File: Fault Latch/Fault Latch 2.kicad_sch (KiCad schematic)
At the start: 113 parts, among them J1 1053141312, J3 1053131202, J4 1053131202, J5 1053131202, K3 Fujitsu_FTR-LYCA005x, K5 Fujitsu_FTR-LYCA005x, K6 Fujitsu_FTR-LYCA005x, Q101 Q_NPN_BEC, Q102 Q_NPN_BEC, Q103 Q_NPN_BEC, Q104 Q_NPN_BEC, Q105 Q_NMOS_GSD, Q106 Q_NMOS_GSD, Q110 Q_NPN_BEC, Q111 Q_NPN_BEC, Q112 Q_NMOS_GSD, Q113 Q_NMOS_GSD, Q114 Q_NMOS_GSD, Q115 Q_NMOS_GSD, Q117 Q_NMOS_GSD, Q118 Q_NMOS_GSD, Q119 Q_NMOS_GSD, Q120 Q_NMOS_GSD, Q121 Q_NMOS_GSD, Q122 Q_NMOS_GSD, Q123 Q_NMOS_GSD, Q124 Q_NMOS_GSD, Q125 Q_NMOS_GSD, SW101 SW_Omron_B3FS, SW102 SW_Omron_B3FS, SW103 SW_Omron_B3FS, U1 74LS279, U104 74AHC1G00, U109 74AHC1G00, U112 74AHC1G00, U117 74AHC1G00, U118 LM555xM, U2 LM1117DT-5.0, U7 SN74AHC1G08DBVR, U8 SN74AHC1G08DBVR

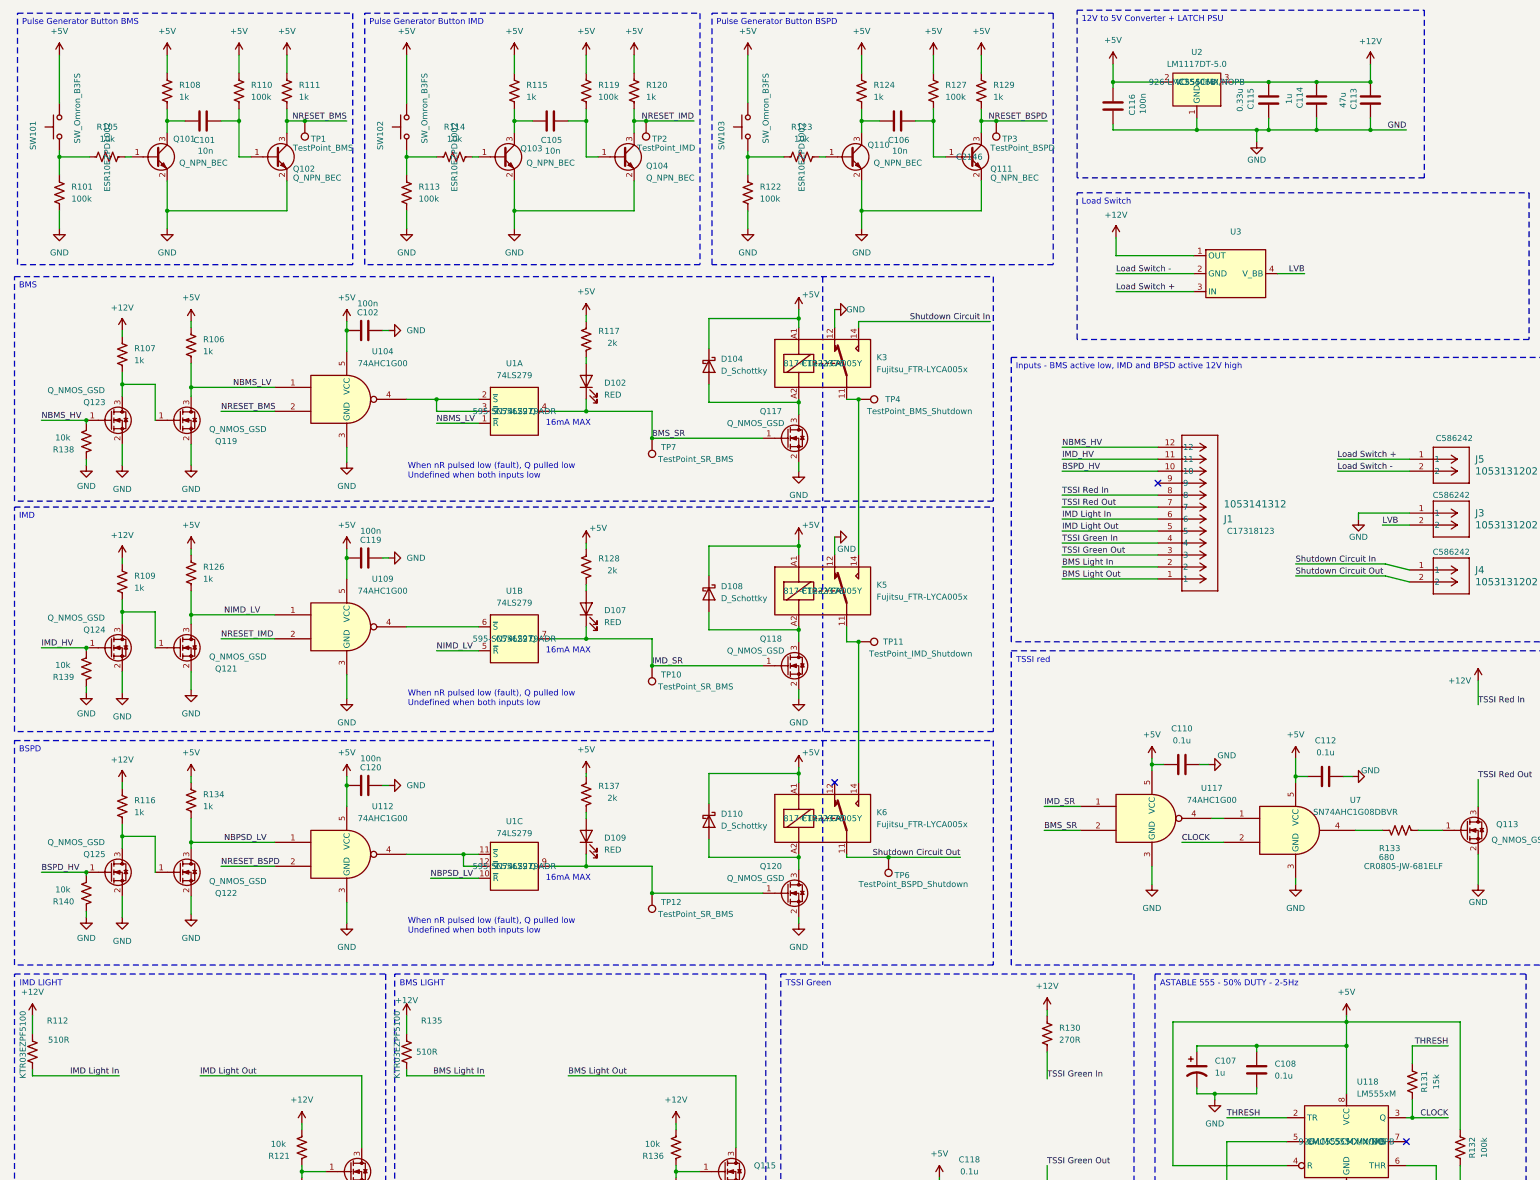
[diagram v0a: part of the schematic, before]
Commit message: Fault Latch reivision
Currently fixing the 2026 iteration of the fault latch.
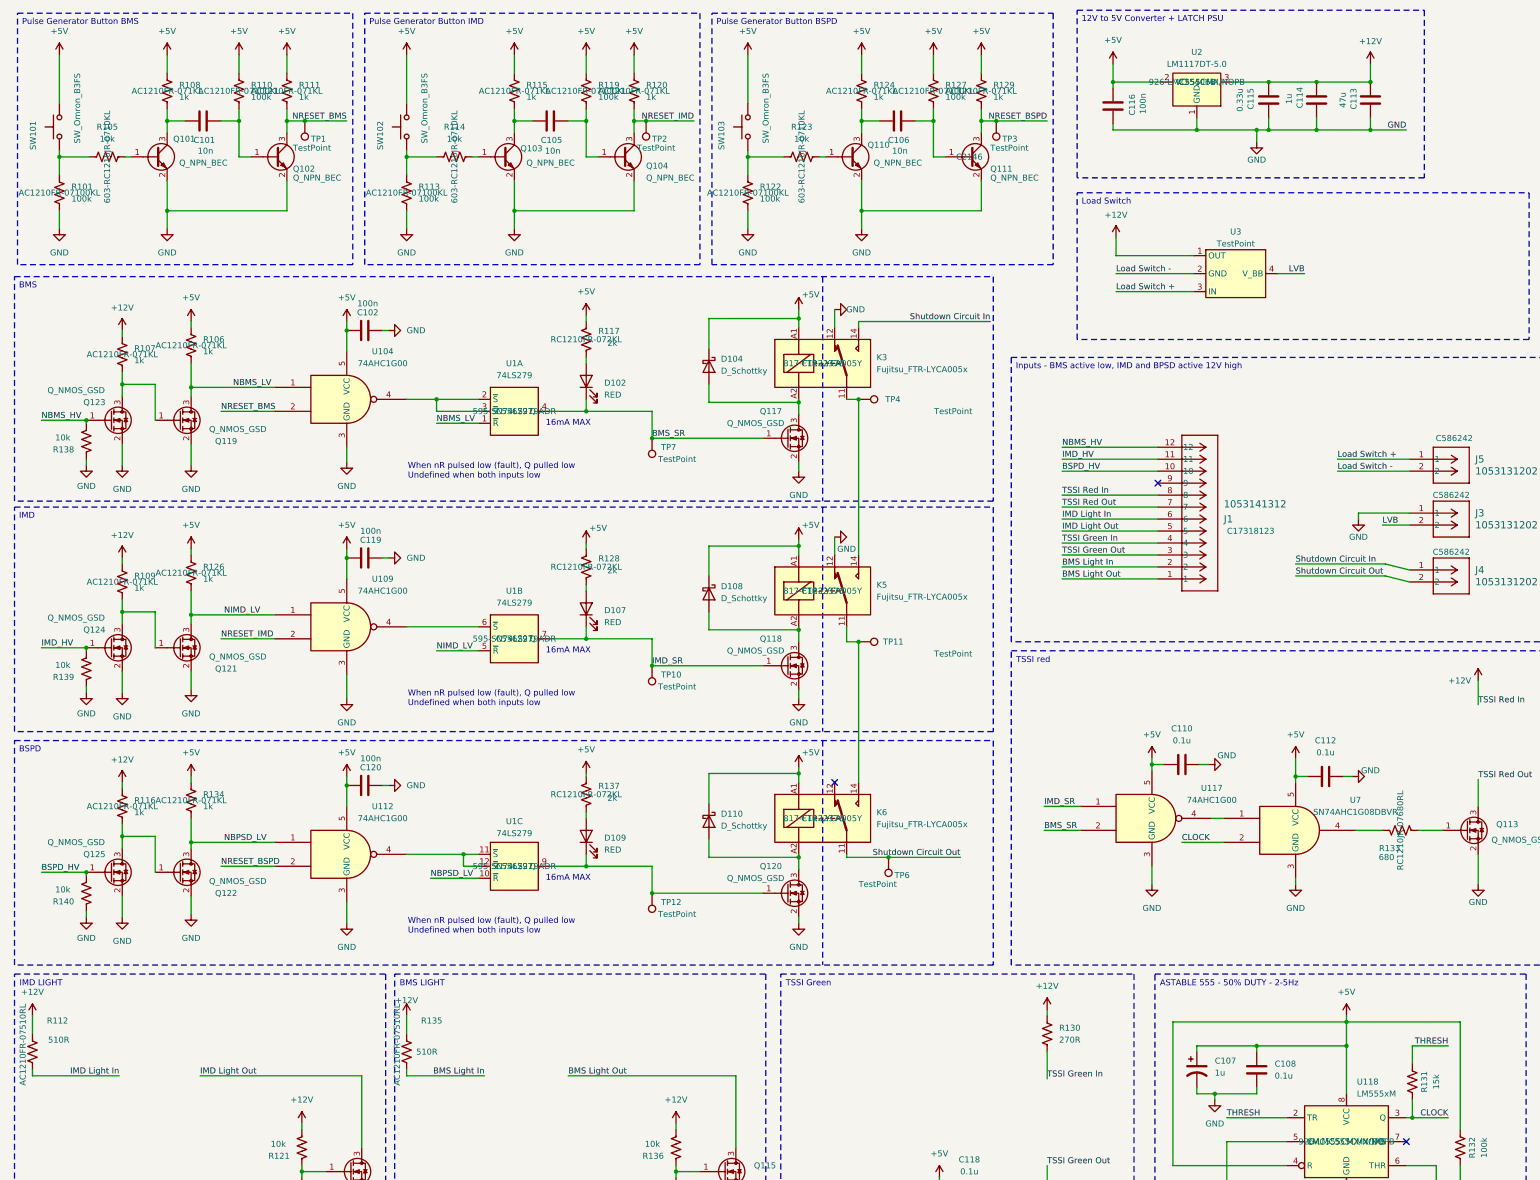
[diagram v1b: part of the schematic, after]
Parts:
- R101, R110, R113, R119, R122, R127: footprint Resistor_SMD:R_0805_2012Metric_Pad1.20x1.40mm_HandSolder -> Resistor_SMD:R_1210_3225Metric; JLC# C149504 -> C230004; MOUSER (none) -> AC1210FR-07100KL
- R105, R114, R121, R123, R136, R138, R139, R140: footprint Resistor_SMD:R_0805_2012Metric_Pad1.20x1.40mm_HandSolder -> Resistor_SMD:R_1210_3225Metric; JLC# C17414 -> C137088; MOUSER ESR10EZPD1002 -> 603-RC1210JR-0710KL
- R106, R107, R109, R116, R126, R134: footprint Resistor_SMD:R_0805_2012Metric_Pad1.20x1.40mm_HandSolder -> Resistor_SMD:R_1210_3225Metric; JLC# C2889437 -> C230096; MOUSER (none) -> AC1210FR-071KL
- R108, R111, R115, R120, R124, R129: footprint Resistor_SMD:R_0805_2012Metric_Pad1.20x1.40mm_HandSolder -> Resistor_SMD:R_1210_3225Metric; JLC# C17513 -> C230096; MOUSER (none) -> AC1210FR-071KL
- R112, R135: footprint Resistor_SMD:R_0603_1608Metric -> Resistor_SMD:R_1210_3225Metric; JLC# KTR03EZPF5100 -> C230277; MOUSER KTR03EZPF5100 -> AC1210FR-07510RL
- R117, R128, R137: footprint Resistor_SMD:R_0805_2012Metric_Pad1.20x1.40mm_HandSolder -> Resistor_SMD:R_1210_3225Metric; JLC# C1359 -> C137097; MOUSER (none) -> RC1210FR-072KL
- R130: footprint Resistor_SMD:R_0603_1608Metric -> Resistor_SMD:R_1210_3225Metric; JLC# C4151887 -> C230144; MOUSER ESR03EZPF2700 -> AC1210FR-07270RL
- R131: footprint Resistor_SMD:R_0603_1608Metric -> Resistor_SMD:R_1210_3225Metric; JLC# C22809 -> C230040; MOUSER (none) -> AC1210FR-0715KL
- R132: footprint Resistor_SMD:R_0603_1608Metric -> Resistor_SMD:R_1210_3225Metric; JLC# C60491 -> C230004; MOUSER (none) -> AC1210FR-07100KL
- R133: footprint Resistor_SMD:R_0805_2012Metric -> Resistor_SMD:R_1210_3225Metric; JLC# C1359 -> C137071; MOUSER (none) -> RC1210JR-07680RL; Manufacturer_Part_Number CR0805-JW-681ELF -> (none)
- TP1: value TestPoint_BMS -> TestPoint
- TP10, TP12, TP7: value TestPoint_SR_BMS -> TestPoint
- TP11: value TestPoint_IMD_Shutdown -> TestPoint
- TP2: value TestPoint_IMD -> TestPoint
- TP3: value TestPoint_BSPD -> TestPoint
- TP4: value TestPoint_BMS_Shutdown -> TestPoint
- TP6: value TestPoint_BSPD_Shutdown -> TestPoint
- U3: value ~ -> TestPoint; footprint Package_TO_SOT_SMD:SOT-223 -> TestPoint:TestPoint_Pad_D1.5mm
